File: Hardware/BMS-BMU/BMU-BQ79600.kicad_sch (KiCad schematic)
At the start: 9 parts, among them U4 BQ79600PWRQ1

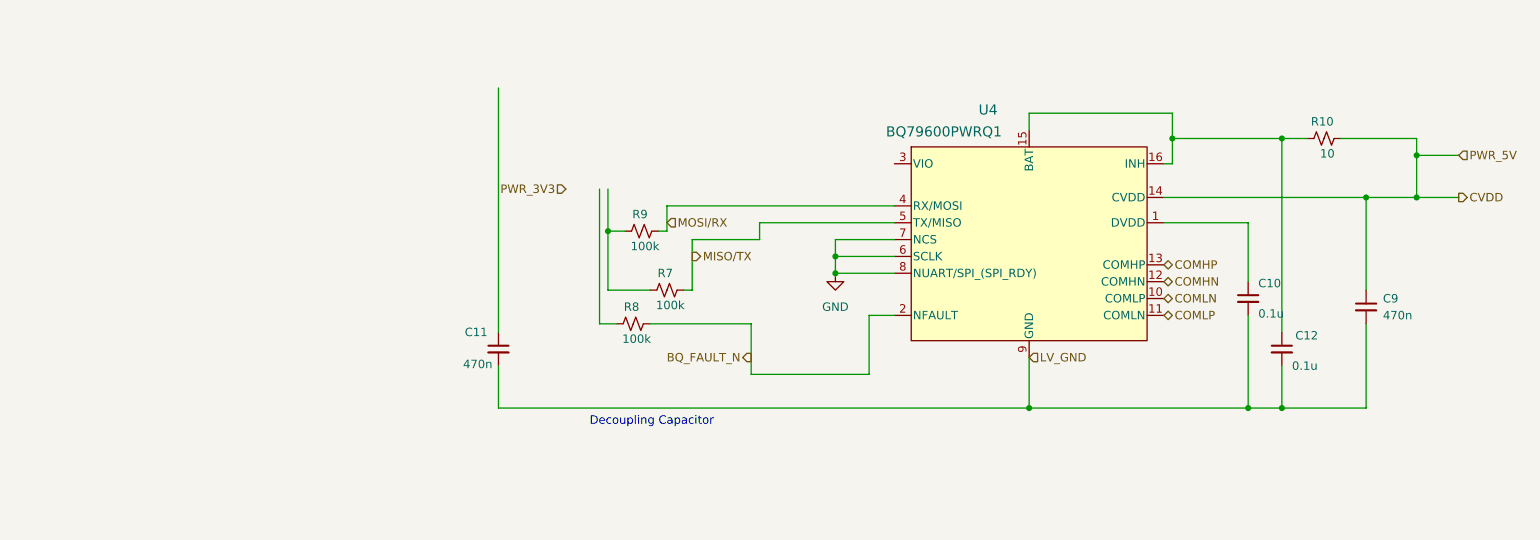
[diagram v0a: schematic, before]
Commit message: update CAN and SHUNT IF
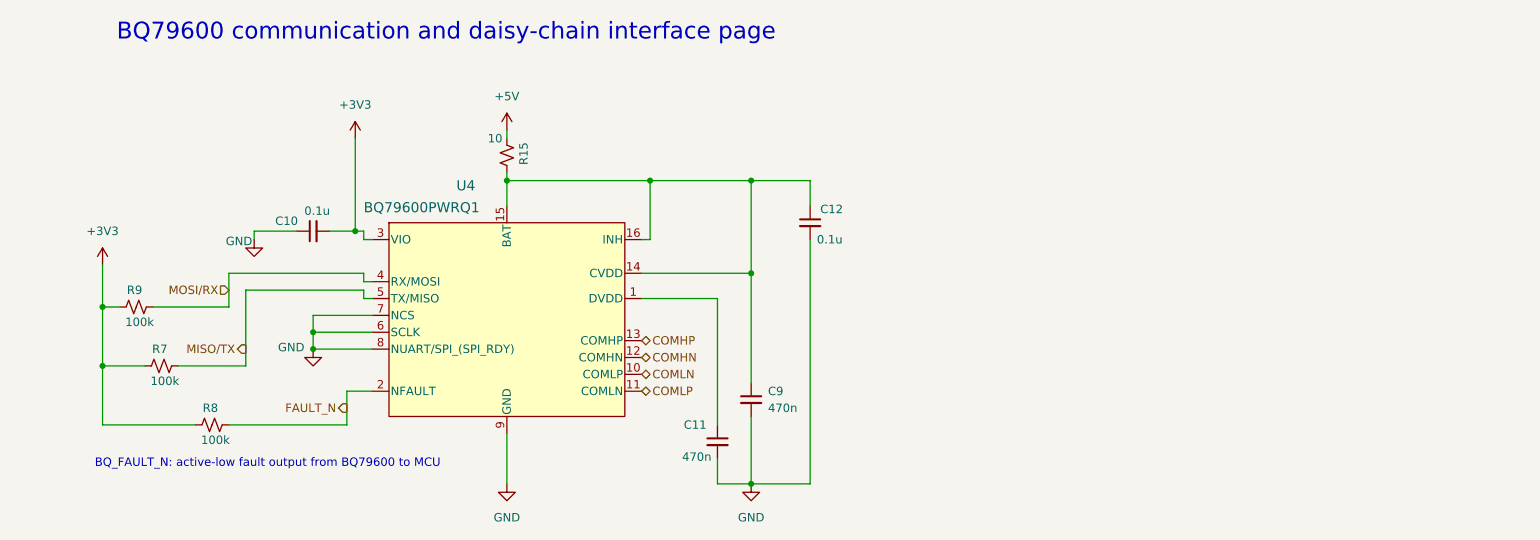
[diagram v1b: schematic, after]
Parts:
- removed R10: 10, symbol Device:R_Small_US
- added R15: 10, symbol Device:R_Small_US
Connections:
- net CVDD is gone; now on an unnamed net: C9.1, U4.14 (CVDD)
- net GND: now also C10.1, C11.2, C12.2, C9.2, U4.9 (GND)
- net +3V3: now reaches R7.1, R9.1
- net +3V3: now also C10.2, R8.1, U4.3 (VIO)
- net at C11.1: now also U4.1 (DVDD)
- net at C12.1, U4.15 (BAT), U4.16 (INH): now also R15.2
- net BQ_FAULT_N renamed FAULT_N
- removed net LV_GND: C10.2, C11.2, C12.2, C9.2, U4.9 (GND)
- new net +5V: R15.1
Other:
- note added: "BQ79600 communication and daisy-chain interface page"
- note added: "BQ_FAULT_N: active-low fault output from BQ79600 to MCU"
- note removed: "Decoupling Capacitor"
- moved on the sheet: C10, C11, C12, C9, R7, R8, R9, U4
